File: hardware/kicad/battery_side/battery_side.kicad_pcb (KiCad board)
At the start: 2 copper layers, 60 x 40 mm, 45 parts, among them J1 Conn_01x02, J2 RJ45, J3 USB-OTG, J5 UART-DBG, Q1 AO3401A, Q2 AO3400A, U1 TPS62933FDRLR, U2 R-78E12-1.0, U3 SN65HVD3082E

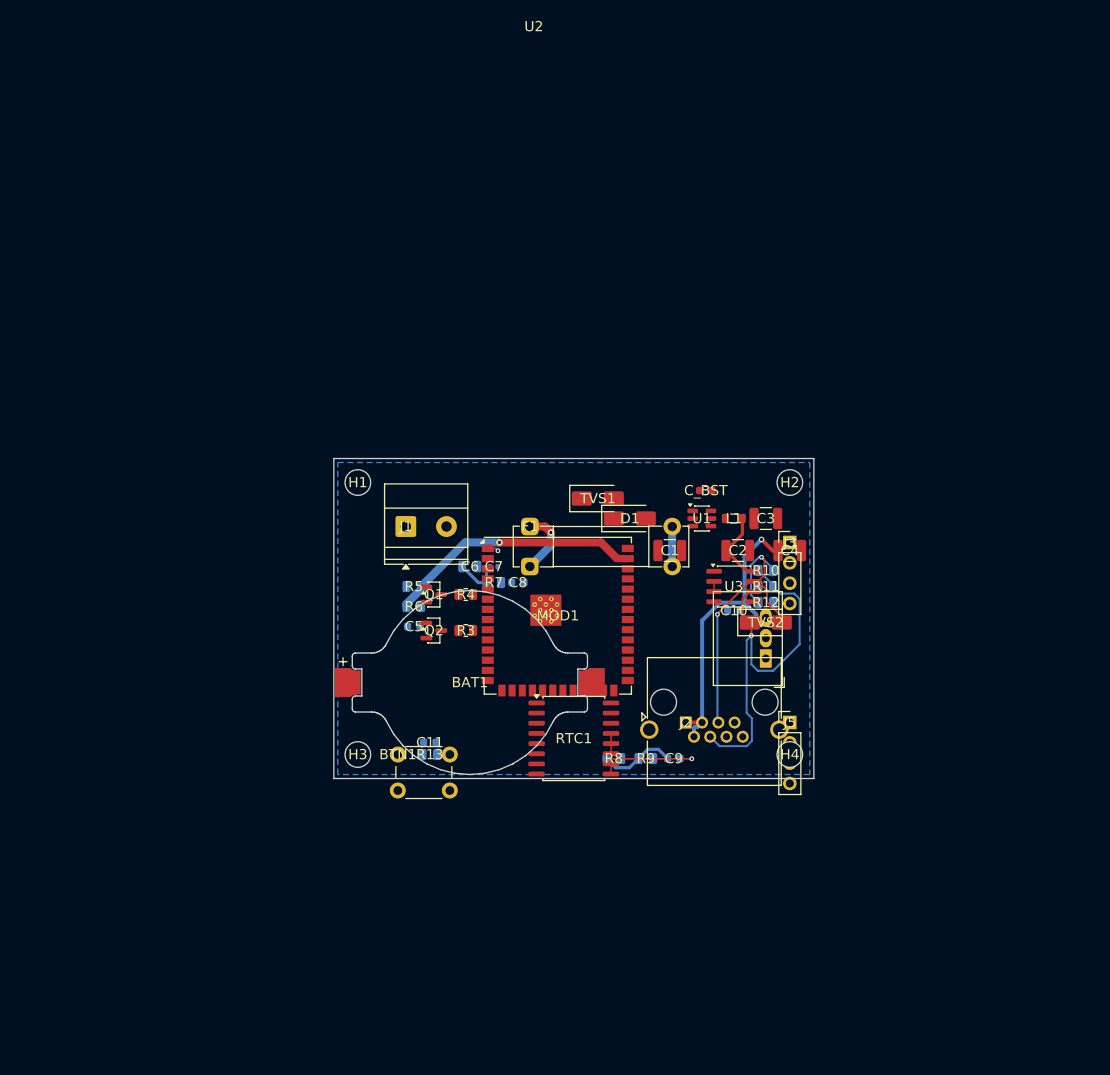
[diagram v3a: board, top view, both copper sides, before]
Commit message: hardware: enlarge battery PCB to 95x75 and re-floorplan (D15)
The 60x40 battery board was over-packed — sub-0.2mm pad clearances,
~28 courtyard overlaps, ~88 silk-over-copper, and the D14 BAT1->MOD1
GPIO short, none independently nudge-fixable. Per D10 (form factor
unconstrained) the board is enlarged to 95x75 (~3x area) and laid out
in functional zones with generous spacing; BAT1 now sits a full band
below MOD1 so its wide CR2032 clips cannot bridge MOD1's GPIO pads.

Build/footprint fixes that fell out of the re-floorplan:
- relocate component Edge.Cuts geometry to F.Fab so BAT1's Keystone_1057
  cell outline no longer corrupts the board outline (invalid_outline +
  edge-clearance) — surface-mount holder, no cutout wanted
- reposition every silk reference via a pcbnew post-process (kiutils
  drops the property (at)/(layer), so refdes printed on the part body);
  hide mounting-hole designators
- place R7 clear of MOD1's PTH thermal-via array
- snapshot/restore the .kicad_pro so the build stops clobbering the
  hand-maintained net classes / DRC severities

Result: 0 error-severity DRC on the placement; remaining 12
drill_out_of_range are MOD1's stock 0.2mm thermal vias (accepted
warnings, D13 convention). Board is unrouted — routing is next.

Co-Authored-By: Claude Opus 4.7 (1M context) <noreply@anthropic.com>
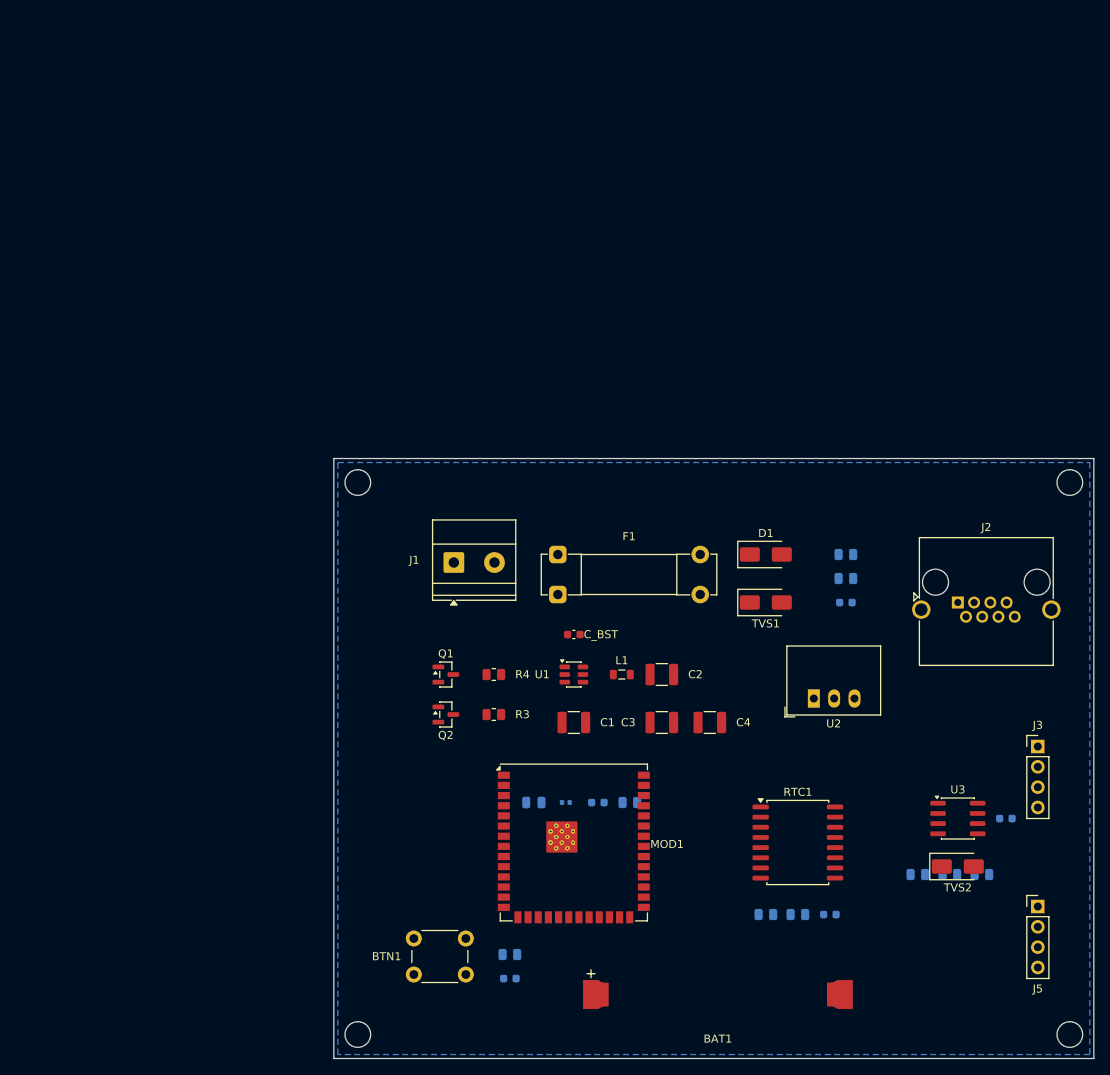
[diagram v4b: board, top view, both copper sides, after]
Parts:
- moved R5 54.1 mm to (64.0, 12.0)
- moved R6 54.1 mm to (64.0, 15.0)
- moved C5 54.1 mm to (64.0, 18.0)
- moved BAT1 49.8 mm to (48.0, 67.0)
- moved H4 49.5 mm to (92.0, 72.0)
- moved R12 43.4 mm to (81.0, 52.0)
- moved C10 42.8 mm to (84.0, 45.0)
- moved R11 42.7 mm to (77.0, 52.0)
- moved R10 42.5 mm to (73.0, 52.0)
- moved U3 40.3 mm to (78.0, 45.0)
- moved J3 40.1 mm to (88.0, 36.0)
- moved TVS2 38.8 mm to (78.0, 51.0)
- moved J5 38.6 mm to (88.0, 56.0)
- moved J2 37.2 mm to (78.0, 18.0)
- moved H2 35.0 mm to (92.0, 3.00)
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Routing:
- net RS485_A: track 50.1 -> 0.00 mm, vias 1 -> 0
- net RS485_B: track 39.3 -> 0.00 mm, vias 2 -> 0
- net V12_CAT5E: track 38.5 -> 0.00 mm, vias 1 -> 0
- net V24_SENSE: track 32.3 -> 0.00 mm, vias 1 -> 0
- net V3V3_SW: track 24.9 -> 0.00 mm
- net GND: track 17.3 -> 0.00 mm, vias 2 -> 0
- net V24_RAW: track 8.28 -> 0.00 mm, vias 1 -> 0
- net V24_AFTER_FUSE: track 5.00 -> 0.00 mm
- net DE_RE: track 1.27 -> 0.00 mm
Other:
- board size 60 x 40 mm -> 95 x 75 mm

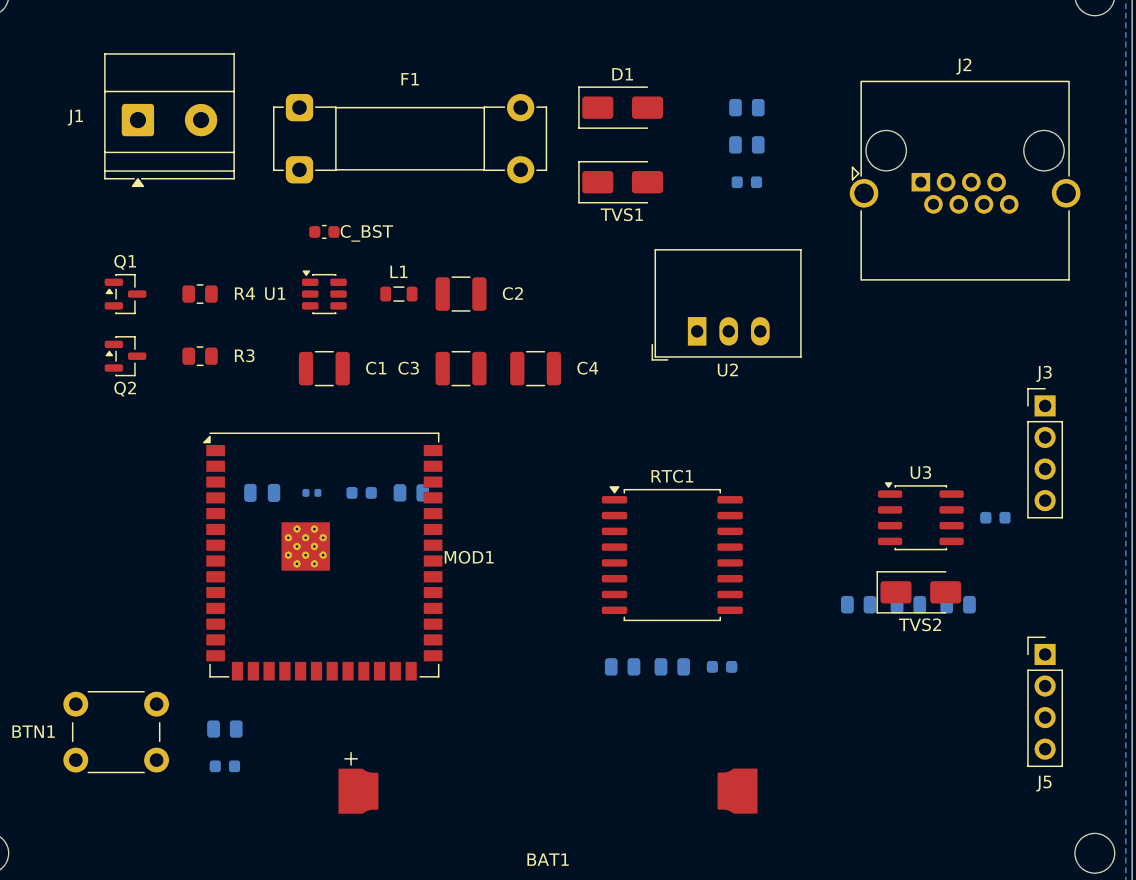
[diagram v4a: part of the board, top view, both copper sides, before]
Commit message: hardware: route battery PCB — 0 error-DRC, 0 unconnected (D15 cont.)
Freerouting v2.1.0 routed all 92 ratsnest connections in 2.7s on the
roomy 95x75 board. Three project-plan items got bound at routing time
(per the CP3 _comment in .kicad_pro about CP4 reinstating numerics):

- Net-class numerics + patterns. _intended_classes_cp4 was a deferred
  placeholder; pcbnew otherwise exported a degenerate Specctra DSN
  (width -0.001 vias) that ballooned Freerouting's maze search until it
  OOMed even at 6GB. Activated Default/Power-{24V,12V,3V3}/RS485-diff
  with their planned track/clearance/via/drill numerics and bound the
  V24_* / V12_* / V3V3* / RS485_* net patterns.
- GND zone connect_pads switched to default thermal reliefs (was
  thru_hole_only — left SMD GND pads requiring manual routing that
  Freerouting reliably missed). Note: kiutils writing an explicit
  "thermal_reliefs" string is invalid KiCad syntax — must be implicit.
- min_resolved_spokes relaxed from 2 to 1 so small bypass caps
  (C8 1uF B.Cu) whose neighbourhood fits only one spoke pass DRC.

Result: 0 error-DRC, 0 unconnected. 21 warnings remain — 12
drill_out_of_range (MOD1 vendor thermal vias), 5 track_dangling (~0.5mm
GND stubs from Freerouting v2.1.0's known-broken multi-thread optimizer),
4 isolated_copper (GND zone fragments >=10 mm^2) — all warning-severity
per D13.

Co-Authored-By: Claude Opus 4.7 (1M context) <noreply@anthropic.com>
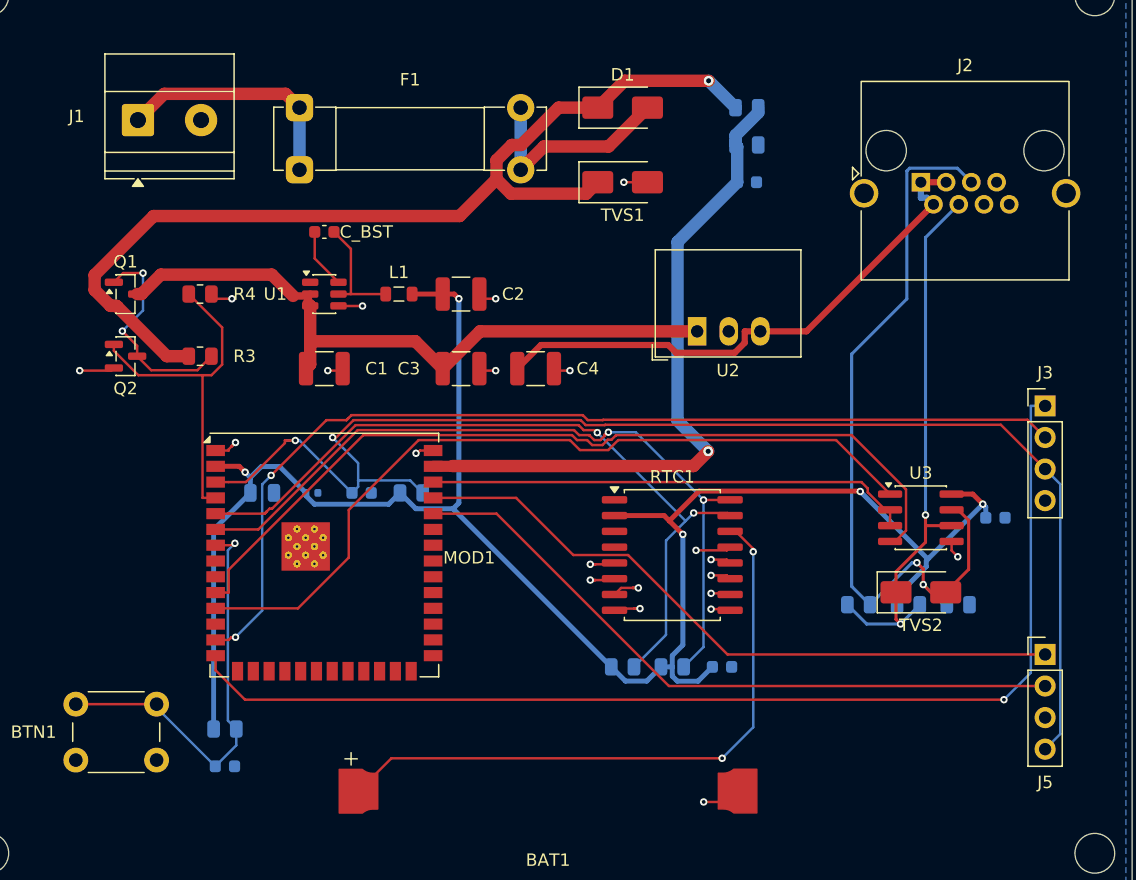
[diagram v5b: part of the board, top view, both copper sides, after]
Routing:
- net V3V3_SW: track 0.00 -> 149.3 mm, vias 0 -> 5
- net ESP_EN: track 0.00 -> 110.2 mm, vias 0 -> 2
- net USB_DP: track 0.00 -> 91.3 mm, vias 0 -> 1
- net USB_DM: track 0.00 -> 81.2 mm, vias 0 -> 2
- net V24_FUSED: track 0.00 -> 79.8 mm, vias 0 -> 1
- net UART_TX_3V3: track 0.00 -> 69.3 mm
- net UART_RX_3V3: track 0.00 -> 64.6 mm
- net RS485_B: track 0.00 -> 63.2 mm, vias 0 -> 2
- net I2C_SCL: track 0.00 -> 61.7 mm, vias 0 -> 2
- net I2C_SDA: track 0.00 -> 61.6 mm, vias 0 -> 2
- net DBG_UART_RX: track 0.00 -> 55.0 mm
- net V24_SW: track 0.00 -> 54.7 mm
- net DBG_UART_TX: track 0.00 -> 54.5 mm
- net V24_SENSE: track 0.00 -> 54.1 mm, vias 0 -> 1
- net V_BAT_RTC: track 0.00 -> 50.6 mm, vias 0 -> 2
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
